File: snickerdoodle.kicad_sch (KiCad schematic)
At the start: 11 parts, among them J2 TFM-115-01-F-D-A, J3 TFM-120-01-F-D-A, U601 TCA9800

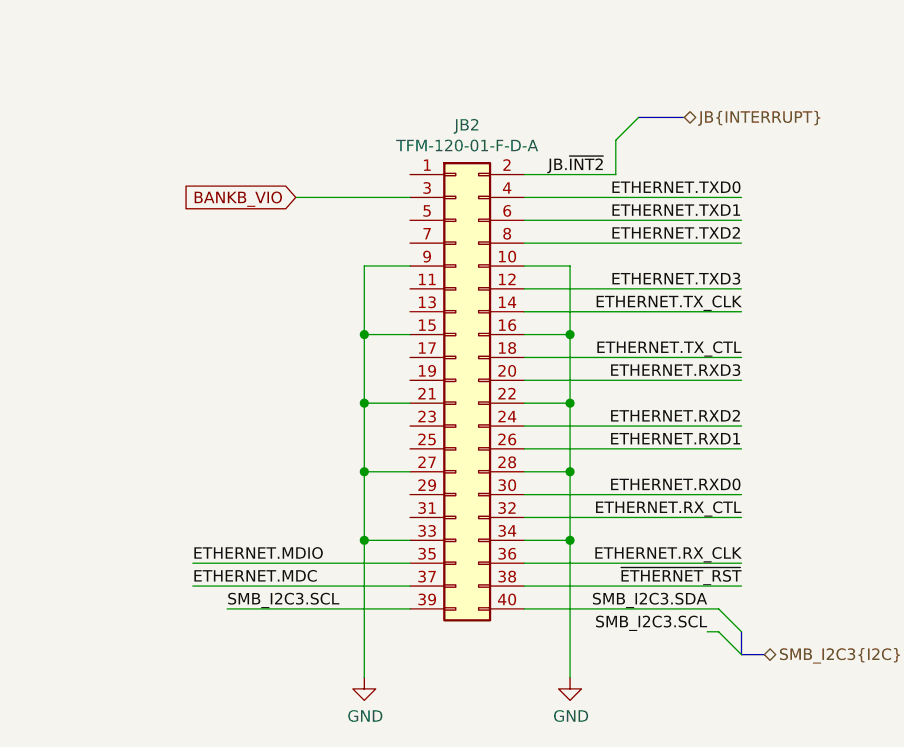
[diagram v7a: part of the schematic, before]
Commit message: Route RGMII signals
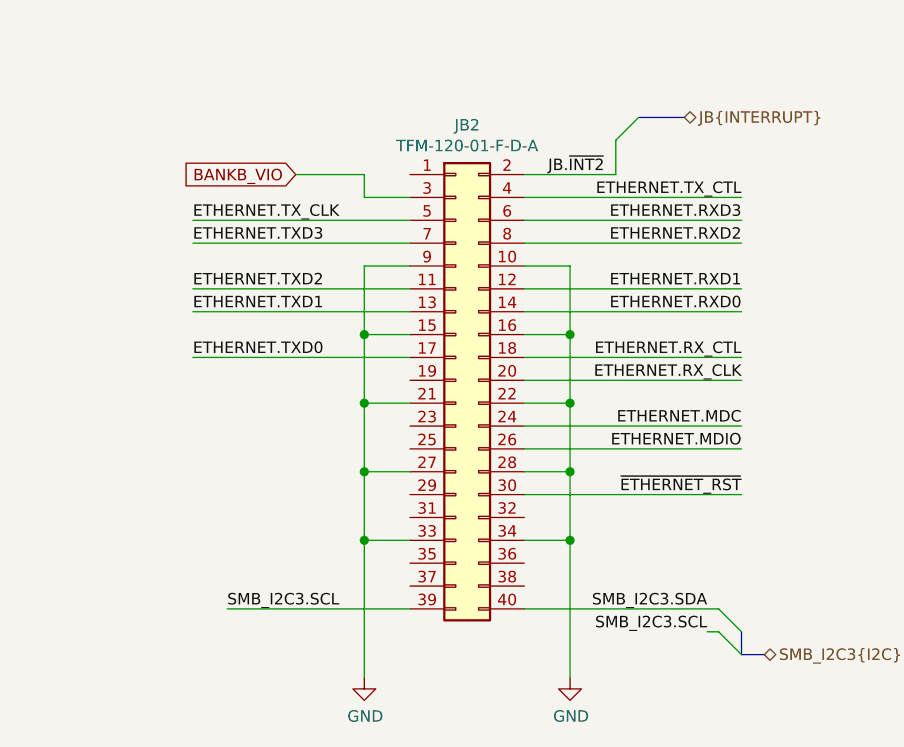
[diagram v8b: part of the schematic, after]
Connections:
- net ETHERNET.MDC: now also JB2.24 (Pin_24); no longer JB2.37 (Pin_37)
- net ETHERNET.MDIO: now also JB2.26 (Pin_26); no longer JB2.35 (Pin_35)
- net ETHERNET.RXD0: now also JB2.14 (Pin_14); no longer JB2.30 (Pin_30)
- net ETHERNET.RXD1: now also JB2.12 (Pin_12); no longer JB2.26 (Pin_26)
- net ETHERNET.RXD2: now also JB2.8 (Pin_8); no longer JB2.24 (Pin_24)
- net ETHERNET.RXD3: now also JB2.6 (Pin_6); no longer JB2.20 (Pin_20)
- net ETHERNET.RX_CLK: now also JB2.20 (Pin_20); no longer JB2.36 (Pin_36)
- net ETHERNET.RX_CTL: now also JB2.18 (Pin_18); no longer JB2.32 (Pin_32)
- net ETHERNET.TXD0: now also JB2.17 (Pin_17); no longer JB2.4 (Pin_4)
- net ETHERNET.TXD1: now also JB2.13 (Pin_13); no longer JB2.6 (Pin_6)
- net ETHERNET.TXD2: now also JB2.11 (Pin_11); no longer JB2.8 (Pin_8)
- net ETHERNET.TXD3: now also JB2.7 (Pin_7); no longer JB2.12 (Pin_12)
- net ETHERNET.TX_CLK: now also JB2.5 (Pin_5); no longer JB2.14 (Pin_14)
- net ETHERNET.TX_CTL: now also JB2.4 (Pin_4); no longer JB2.18 (Pin_18)
- net ~ETHERNET_RST: now also JB2.30 (Pin_30); no longer JB2.38 (Pin_38)
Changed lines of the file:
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@@
   )
   (bus_alias "JTAG" (members "TDI" "TDO" "TCK" "TMS" "ZYNQ_~RST" "PGND"))
+  (bus_alias "I2C" (members "SDA" "SCL"))
   (bus_alias "SWD" (members "MCU_~RST" "SWCLK" "SWDIO"))
-  (bus_alias "I2C" (members "SDA" "SCL"))
   (bus_alias "INTERRUPT" (members "~INT1" "~INT2"))
   (junction (at 48.26 45.72) (diameter 1.016) (color 0 0 0 0))
@@
     (stroke (width 0) (type solid) (color 0 0 0 0))
   )
-  (wire (pts (xy 140.97 165.1) (xy 153.67 165.1))
+  (wire (pts (xy 140.97 162.56) (xy 148.59 162.56))
     (stroke (width 0) (type solid) (color 0 0 0 0))
   )
@@
     (stroke (width 0) (type solid) (color 0 0 0 0))
   )
+  (wire (pts (xy 148.59 162.56) (xy 148.59 165.1))
+    (stroke (width 0) (type solid) (color 0 0 0 0))
+  )
+  (wire (pts (xy 148.59 165.1) (xy 153.67 165.1))
+    (stroke (width 0) (type solid) (color 0 0 0 0))
+  )
   (wire (pts (xy 148.59 172.72) (xy 148.59 180.34))
     (stroke (width 0) (type solid) (color 0 0 0 0))
@@
     (stroke (width 0) (type solid) (color 0 0 0 0))
   )
+  (wire (pts (xy 153.67 167.64) (xy 129.54 167.64))
+    (stroke (width 0) (type solid) (color 0 0 0 0))
+  )
+  (wire (pts (xy 153.67 170.18) (xy 129.54 170.18))
+    (stroke (width 0) (type solid) (color 0 0 0 0))
+  )
+  (wire (pts (xy 153.67 175.26) (xy 129.54 175.26))
+    (stroke (width 0) (type solid) (color 0 0 0 0))
+  )
+  (wire (pts (xy 153.67 177.8) (xy 129.54 177.8))
+    (stroke (width 0) (type solid) (color 0 0 0 0))
+  )
   (wire (pts (xy 153.67 180.34) (xy 148.59 180.34))
     (stroke (width 0) (type solid) (color 0 0 0 0))
   )
+  (wire (pts (xy 153.67 182.88) (xy 129.54 182.88))
+    (stroke (width 0) (type solid) (color 0 0 0 0))
+  )
   (wire (pts (xy 153.67 187.96) (xy 148.59 187.96))
     (stroke (width 0) (type solid) (color 0 0 0 0))
@@
     (stroke (width 0) (type solid) (color 0 0 0 0))
   )
-  (wire (pts (xy 153.67 205.74) (xy 129.54 205.74))
-    (stroke (width 0) (type solid) (color 0 0 0 0))
-  )
-  (wire (pts (xy 153.67 208.28) (xy 129.54 208.28))
-    (stroke (width 0) (type solid) (color 0 0 0 0))
-  )
   (wire (pts (xy 166.37 27.94) (xy 177.8 27.94))
     (stroke (width 0) (type solid) (color 0 0 0 0))
@@
     (stroke (width 0) (type solid) (color 0 0 0 0))
   )
-  (wire (pts (xy 166.37 167.64) (xy 190.5 167.64))
-    (stroke (width 0) (type solid) (color 0 0 0 0))
-  )
-  (wire (pts (xy 166.37 170.18) (xy 190.5 170.18))
-    (stroke (width 0) (type solid) (color 0 0 0 0))
-  )
-  (wire (pts (xy 166.37 175.26) (xy 190.5 175.26))
-    (stroke (width 0) (type solid) (color 0 0 0 0))
-  )
-  (wire (pts (xy 166.37 177.8) (xy 190.5 177.8))
-    (stroke (width 0) (type solid) (color 0 0 0 0))
-  )
   (wire (pts (xy 166.37 180.34) (xy 171.45 180.34))
     (stroke (width 0) (type solid) (color 0 0 0 0))
   )
-  (wire (pts (xy 166.37 182.88) (xy 190.5 182.88))
-    (stroke (width 0) (type solid) (color 0 0 0 0))
-  )
   (wire (pts (xy 166.37 187.96) (xy 171.45 187.96))
     (stroke (width 0) (type solid) (color 0 0 0 0))
   )
+  (wire (pts (xy 166.37 190.5) (xy 190.5 190.5))
+    (stroke (width 0) (type solid) (color 0 0 0 0))
+  )
+  (wire (pts (xy 166.37 193.04) (xy 190.5 193.04))
+    (stroke (width 0) (type solid) (color 0 0 0 0))
+  )
+  (wire (pts (xy 166.37 198.12) (xy 190.5 198.12))
+    (stroke (width 0) (type solid) (color 0 0 0 0))
+  )
   (wire (pts (xy 166.37 203.2) (xy 171.45 203.2))
     (stroke (width 0) (type solid) (color 0 0 0 0))
   )
-  (wire (pts (xy 166.37 208.28) (xy 190.5 208.28))
-    (stroke (width 0) (type solid) (color 0 0 0 0))
-  )
   (wire (pts (xy 166.37 210.82) (xy 187.96 210.82))
     (stroke (width 0) (type solid) (color 0 0 0 0))
@@
     (stroke (width 0) (type solid) (color 0 0 0 0))
   )
+  (wire (pts (xy 190.5 167.64) (xy 166.37 167.64))
+    (stroke (width 0) (type solid) (color 0 0 0 0))
+  )
+  (wire (pts (xy 190.5 170.18) (xy 166.37 170.18))
+    (stroke (width 0) (type solid) (color 0 0 0 0))
+  )
+  (wire (pts (xy 190.5 175.26) (xy 166.37 175.26))
+    (stroke (width 0) (type solid) (color 0 0 0 0))
+  )
+  (wire (pts (xy 190.5 177.8) (xy 166.37 177.8))
+    (stroke (width 0) (type solid) (color 0 0 0 0))
+  )
+  (wire (pts (xy 190.5 182.88) (xy 166.37 182.88))
+    (stroke (width 0) (type solid) (color 0 0 0 0))
+  )
   (wire (pts (xy 190.5 185.42) (xy 166.37 185.42))
     (stroke (width 0) (type solid) (color 0 0 0 0))
   )
-  (wire (pts (xy 190.5 190.5) (xy 166.37 190.5))
-    (stroke (width 0) (type solid) (color 0 0 0 0))
-  )
-  (wire (pts (xy 190.5 193.04) (xy 166.37 193.04))
-    (stroke (width 0) (type solid) (color 0 0 0 0))
-  )
-  (wire (pts (xy 190.5 198.12) (xy 166.37 198.12))
-    (stroke (width 0) (type solid) (color 0 0 0 0))
-  )
-  (wire (pts (xy 190.5 200.66) (xy 166.37 200.66))
-    (stroke (width 0) (type solid) (color 0 0 0 0))
-  )
-  (wire (pts (xy 190.5 205.74) (xy 166.37 205.74))
-    (stroke (width 0) (type solid) (color 0 0 0 0))
-  )
   (wire (pts (xy 231.14 196.85) (xy 231.14 199.39))
     (stroke (width 0) (type solid) (color 0 0 0 0))
@@
     (effects (font (size 1.27 1.27)) (justify right bottom))
   )
-  (label "ETHERNET.MDIO" (at 129.54 205.74 0)
-    (effects (font (size 1.27 1.27)) (justify left bottom))
-  )
-  (label "ETHERNET.MDC" (at 129.54 208.28 0)
+  (label "ETHERNET.TX_CLK" (at 129.54 167.64 0)
+    (effects (font (size 1.27 1.27)) (justify left bottom))
+  )
+  (label "ETHERNET.TXD3" (at 129.54 170.18 0)
+    (effects (font (size 1.27 1.27)) (justify left bottom))
+  )
+  (label "ETHERNET.TXD2" (at 129.54 175.26 0)
+    (effects (font (size 1.27 1.27)) (justify left bottom))
+  )
+  (label "ETHERNET.TXD1" (at 129.54 177.8 0)
+    (effects (font (size 1.27 1.27)) (justify left bottom))
+  )
+  (label "ETHERNET.TXD0" (at 129.54 182.88 0)
     (effects (font (size 1.27 1.27)) (justify left bottom))
   )
@@
     (effects (font (size 1.27 1.27)) (justify right bottom))
   )
-  (label "ETHERNET.TXD0" (at 190.5 165.1 180)
-    (effects (font (size 1.27 1.27)) (justify right bottom))
-  )
-  (label "ETHERNET.TXD1" (at 190.5 167.64 180)
-    (effects (font (size 1.27 1.27)) (justify right bottom))
-  )
-  (label "ETHERNET.TXD2" (at 190.5 170.18 180)
-    (effects (font (size 1.27 1.27)) (justify right bottom))
-  )
-  (label "ETHERNET.TXD3" (at 190.5 175.26 180)
-    (effects (font (size 1.27 1.27)) (justify right bottom))
-  )
-  (label "ETHERNET.TX_CLK" (at 190.5 177.8 180)
-    (effects (font (size 1.27 1.27)) (justify right bottom))
-  )
-  (label "ETHERNET.TX_CTL" (at 190.5 182.88 180)
-    (effects (font (size 1.27 1.27)) (justify right bottom))
-  )
-  (label "ETHERNET.RXD3" (at 190.5 185.42 180)
-    (effects (font (size 1.27 1.27)) (justify right bottom))
-  )
-  (label "ETHERNET.RXD2" (at 190.5 190.5 180)
-    (effects (font (size 1.27 1.27)) (justify right bottom))
-  )
-  (label "ETHERNET.RXD1" (at 190.5 193.04 180)
-    (effects (font (size 1.27 1.27)) (justify right bottom))
-  )
-  (label "ETHERNET.RXD0" (at 190.5 198.12 180)
-    (effects (font (size 1.27 1.27)) (justify right bottom))
-  )
-  (label "ETHERNET.RX_CTL" (at 190.5 200.66 180)
-    (effects (font (size 1.27 1.27)) (justify right bottom))
-  )
-  (label "ETHERNET.RX_CLK" (at 190.5 205.74 180)
-    (effects (font (size 1.27 1.27)) (justify right bottom))
-  )
-  (label "~ETHERNET_RST" (at 190.5 208.28 180)
+  (label "ETHERNET.TX_CTL" (at 190.5 165.1 180)
+    (effects (font (size 1.27 1.27)) (justify right bottom))
+  )
+  (label "ETHERNET.RXD3" (at 190.5 167.64 180)
+    (effects (font (size 1.27 1.27)) (justify right bottom))
+  )
+  (label "ETHERNET.RXD2" (at 190.5 170.18 180)
+    (effects (font (size 1.27 1.27)) (justify right bottom))
+  )
+  (label "ETHERNET.RXD1" (at 190.5 175.26 180)
+    (effects (font (size 1.27 1.27)) (justify right bottom))
+  )
+  (label "ETHERNET.RXD0" (at 190.5 177.8 180)
+    (effects (font (size 1.27 1.27)) (justify right bottom))
+  )
+  (label "ETHERNET.RX_CTL" (at 190.5 182.88 180)
+    (effects (font (size 1.27 1.27)) (justify right bottom))
+  )
+  (label "ETHERNET.RX_CLK" (at 190.5 185.42 180)
+    (effects (font (size 1.27 1.27)) (justify right bottom))
+  )
+  (label "ETHERNET.MDC" (at 190.5 190.5 180)
+    (effects (font (size 1.27 1.27)) (justify right bottom))
+  )
+  (label "ETHERNET.MDIO" (at 190.5 193.04 180)
+    (effects (font (size 1.27 1.27)) (justify right bottom))
+  )
+  (label "~ETHERNET_RST" (at 190.5 198.12 180)
     (effects (font (size 1.27 1.27)) (justify right bottom))
   )
@@
     (effects (font (size 1.27 1.27)) (justify right))
   )
-  (global_label "BANKB_VIO" (shape input) (at 140.97 165.1 180)
+  (global_label "BANKB_VIO" (shape input) (at 140.97 162.56 180)
     (effects (font (size 1.27 1.27)) (justify right))
   )
